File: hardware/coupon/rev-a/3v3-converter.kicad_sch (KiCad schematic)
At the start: 9 parts, among them U36 TPS631000DRLR

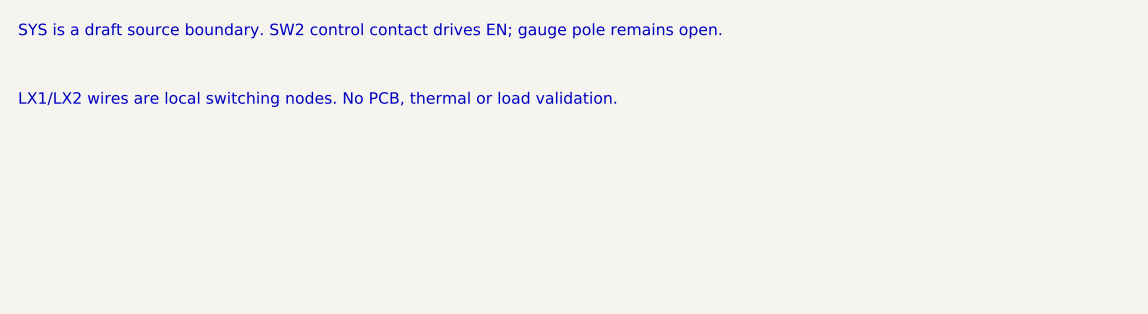
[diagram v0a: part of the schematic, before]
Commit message: Connect switched gauge through isolated I2C buffer
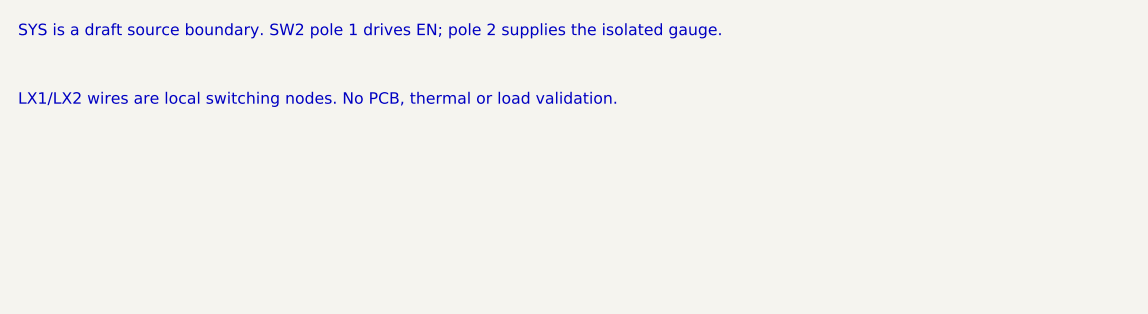
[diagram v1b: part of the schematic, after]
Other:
- note added: "SYS is a draft source boundary. SW2 pole 1 drives EN; pole 2 supplies the isolated gauge."
- note removed: "SYS is a draft source boundary. SW2 control contact drives EN; gauge pole remains open."
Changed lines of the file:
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@@
 (paper "A3")
 (title_block (title "Coupon Rev A - provisional 3V3 application converter") (rev "A-draft") (comment 1 "SPDX-License-Identifier: CERN-OHL-S-2.0") (comment 2 "SYS source draft; physical switch control linked; no fabrication"))
-(text "SYS is a draft source boundary. SW2 control contact drives EN; gauge pole remains open." (at 20.320 20.320 0) (effects (font (size 1.27 1.27)) (justify left)))
+(text "SYS is a draft source boundary. SW2 pole 1 drives EN; pole 2 supplies the isolated gauge." (at 20.320 20.320 0) (effects (font (size 1.27 1.27)) (justify left)))
 (text "LX1/LX2 wires are local switching nodes. No PCB, thermal or load validation." (at 20.320 27.940 0) (effects (font (size 1.27 1.27)) (justify left)))
 (symbol (lib_id "rgb-badge-coupon:TPS631000DRLR") (at 147.320 96.520 0) (unit 1)
